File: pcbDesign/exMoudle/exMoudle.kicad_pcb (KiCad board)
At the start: 2 copper layers, 56 x 133 mm, 23 parts, among them J1 luat-esp32-s3_socket, J2 face recognition, J3 Lidar, SW1 SW_Push, SW10 SW_Push, SW11 SW_Push, SW12 SW_Push, SW2 SW_Push, SW3 SW_Push, SW4 SW_Push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

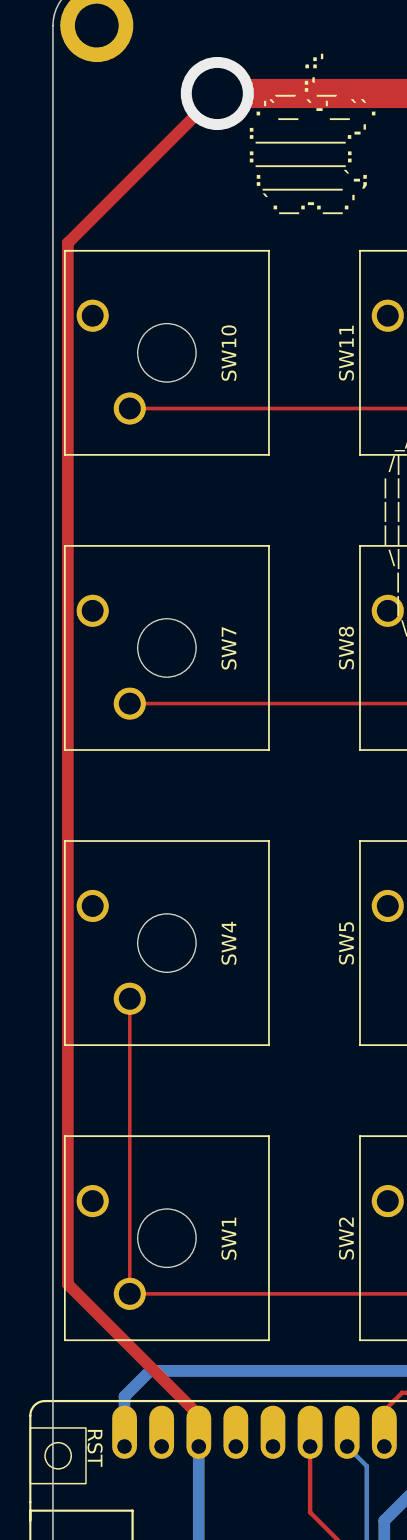
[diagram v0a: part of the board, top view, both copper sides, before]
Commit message: update exModule pcb layout
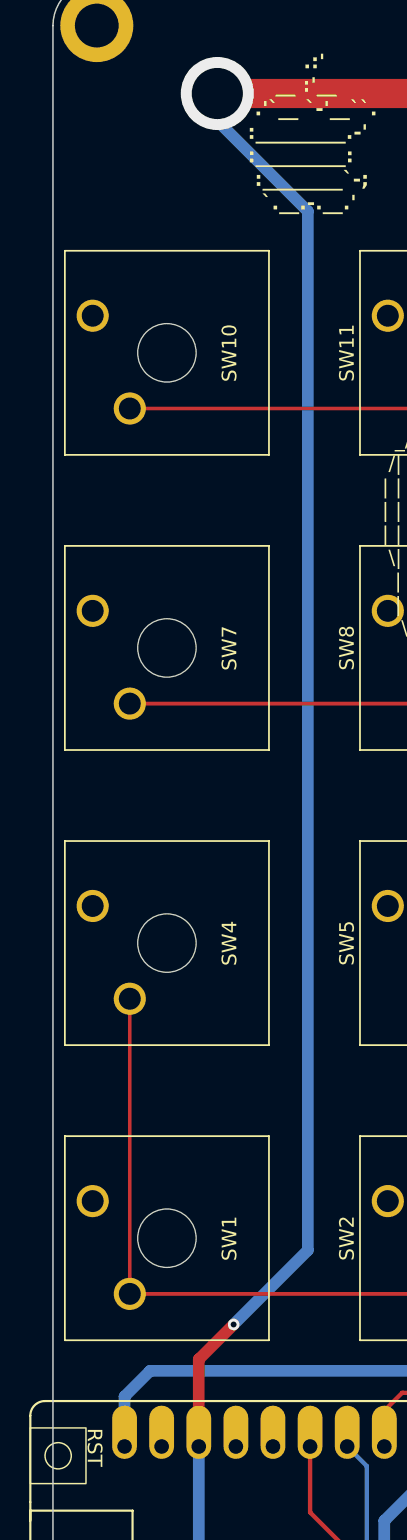
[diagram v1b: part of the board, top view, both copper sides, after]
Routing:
- net GND: track 276.0 -> 274.5 mm, vias 3 -> 4
